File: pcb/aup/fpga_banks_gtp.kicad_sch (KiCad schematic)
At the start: 1 part, among them U1 XC7A50T-2FGG484C

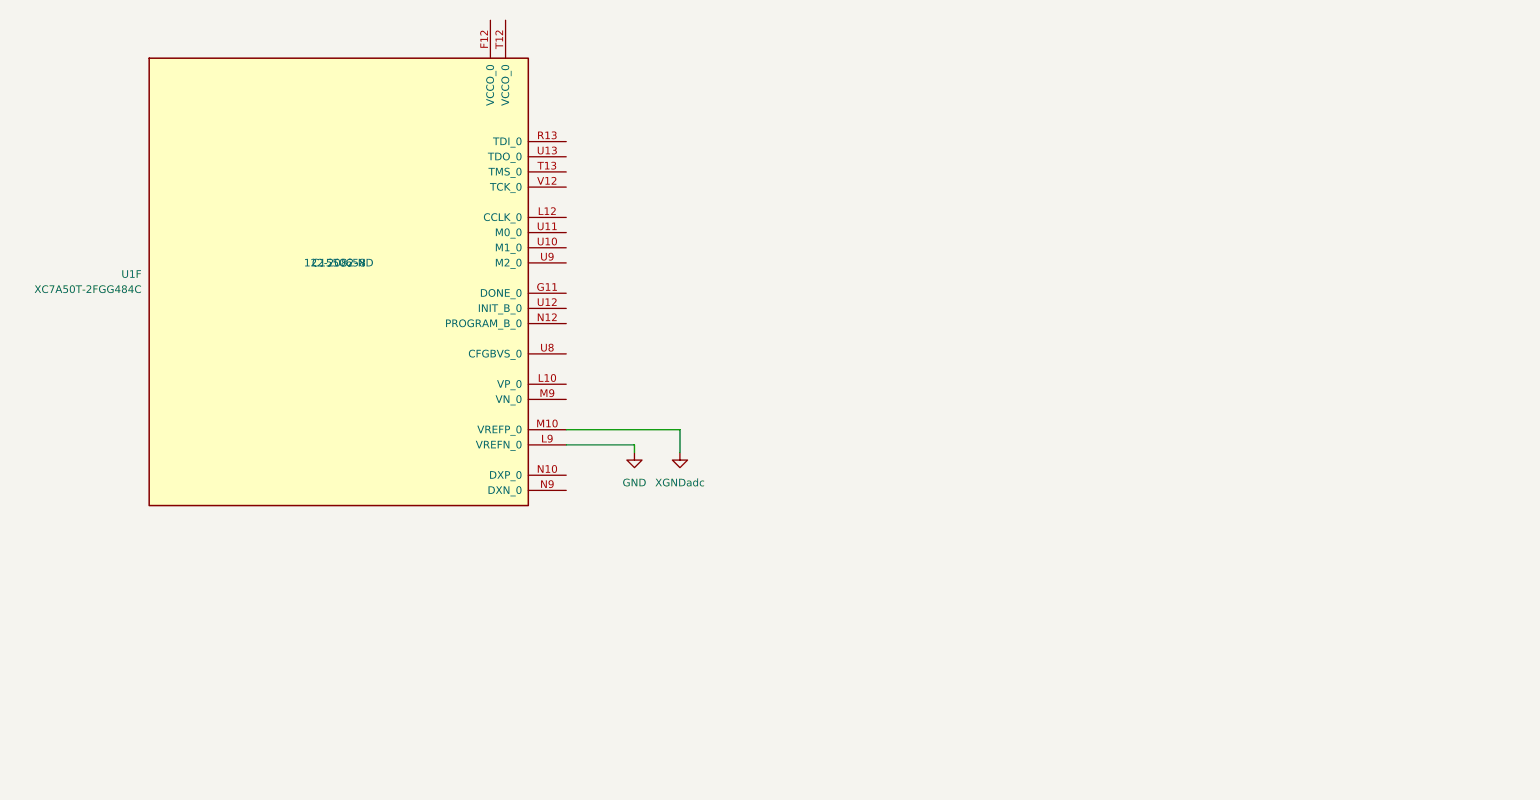
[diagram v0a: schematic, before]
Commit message: Add hierarchical sheets for banks and add caps.
There are some stale sheets in this commit, but I don't want to delete
an active one accidentally. Save them all for now, and then go back and
clean them up.
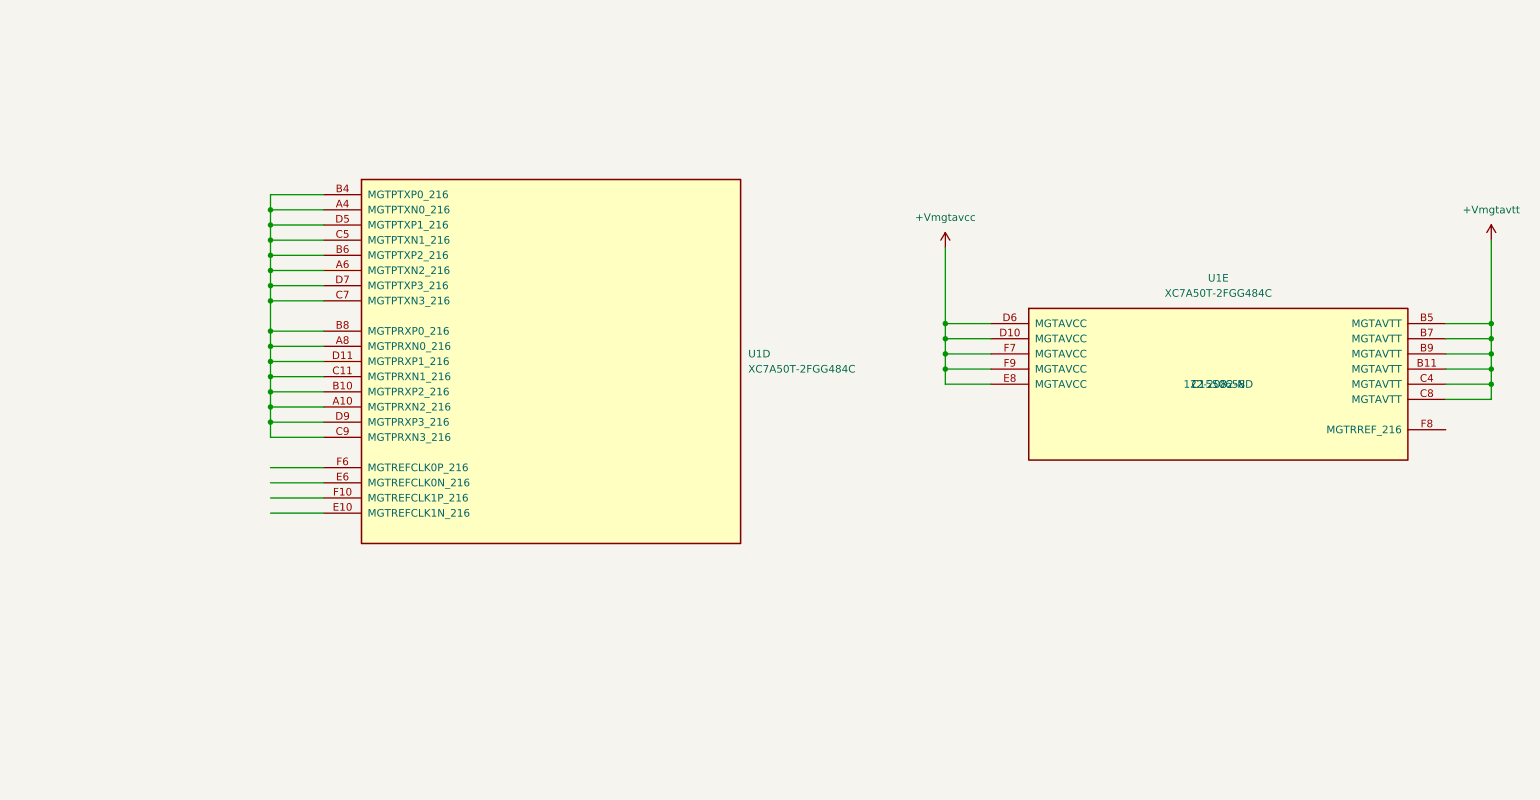
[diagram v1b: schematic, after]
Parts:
- removed U1: XC7A50T-2FGG484C, !Xilinx:Xilinx_FGG484, symbol !Xilinx:XC7A50T-FGG484
- added U1: XC7A50T-2FGG484C, !Xilinx:Xilinx_FGG484, symbol !Xilinx:XC7A50T-FGG484
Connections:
- new net: U1.A10 (MGTPRXN2_216), U1.A4 (MGTPTXN0_216), U1.A6 (MGTPTXN2_216), U1.A8 (MGTPRXN0_216), U1.B10 (MGTPRXP2_216), U1.B4 (MGTPTXP0_216), U1.B6 (MGTPTXP2_216), U1.B8 (MGTPRXP0_216), U1.C11 (MGTPRXN1_216), U1.C5 (MGTPTXN1_216), U1.C7 (MGTPTXN3_216), U1.C9 (MGTPRXN3_216), U1.D11 (MGTPRXP1_216), U1.D5 (MGTPTXP1_216), U1.D7 (MGTPTXP3_216), U1.D9 (MGTPRXP3_216)
- new net +Vmgtavcc: U1.D10 (MGTAVCC), U1.D6 (MGTAVCC), U1.E8 (MGTAVCC), U1.F7 (MGTAVCC), U1.F9 (MGTAVCC)
- new net +Vmgtavtt: U1.B11 (MGTAVTT), U1.B5 (MGTAVTT), U1.B7 (MGTAVTT), U1.B9 (MGTAVTT), U1.C4 (MGTAVTT), U1.C8 (MGTAVTT)

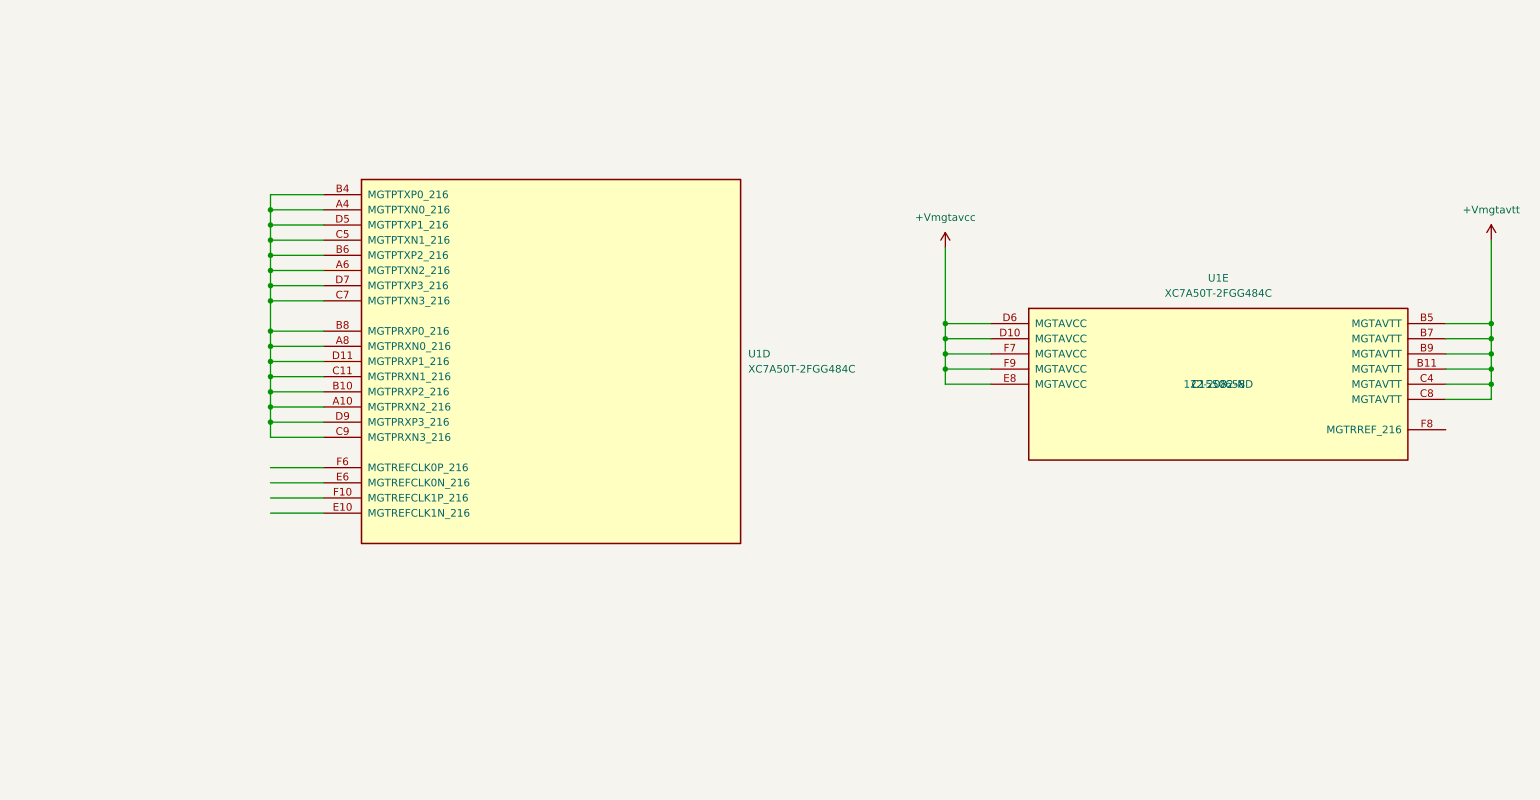
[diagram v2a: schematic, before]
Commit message: Add GTP passives
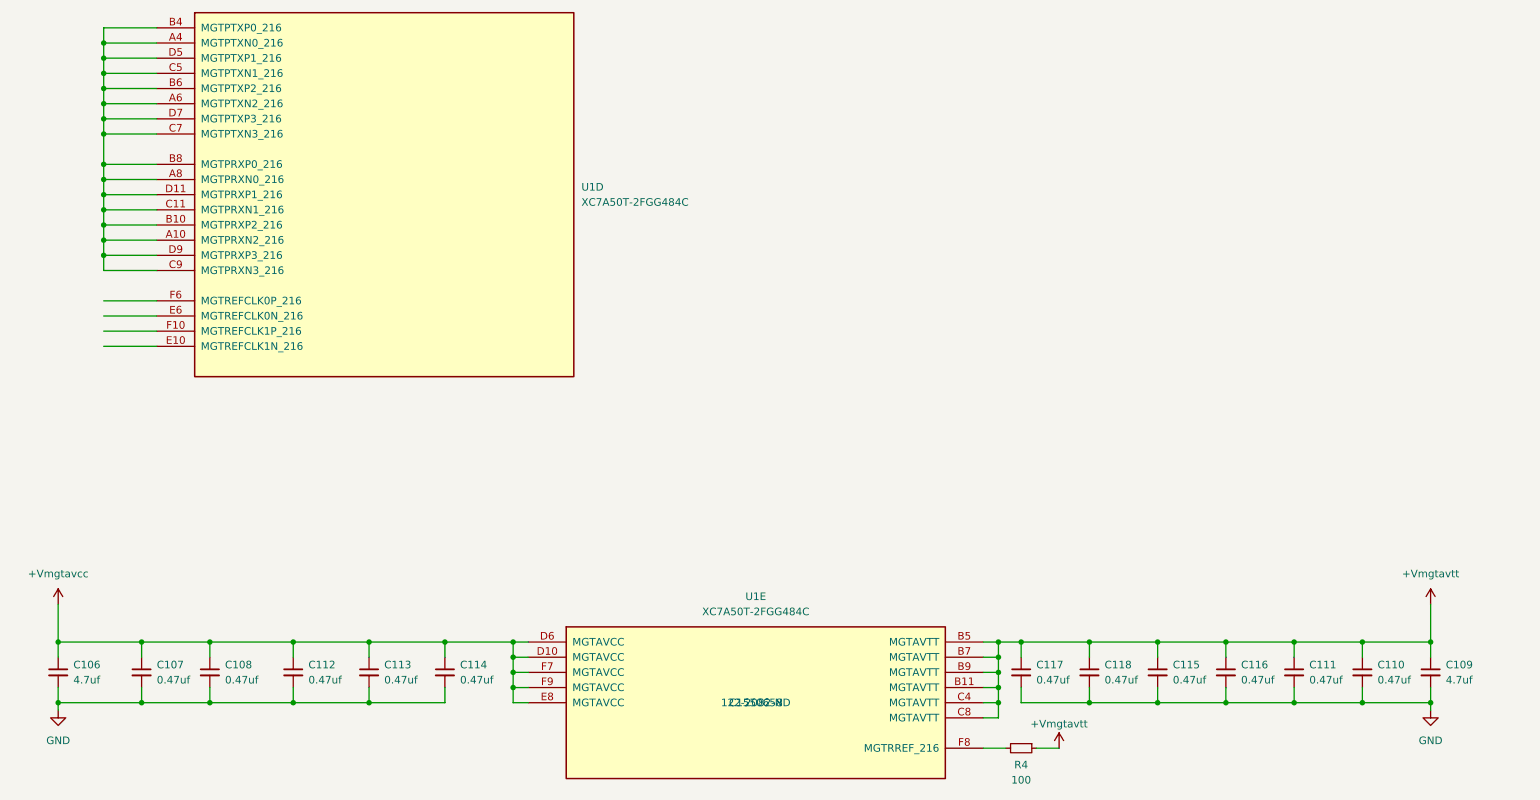
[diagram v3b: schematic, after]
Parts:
- added C106, C109: 4.7uf, Capacitor_SMD:C_0805_2012Metric, symbol !Misc:C_4.7uf_0805
- added C107, C108, C110, C111, C112, C113, C114, C115, C116, C117, C118: 0.47uf, Capacitor_SMD:C_0201_0603Metric, symbol !Misc:C_0.47uf_0201
- added R4: 100, Resistor_SMD:R_0201_0603Metric, symbol !Misc:R_100_0201
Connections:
- net +Vmgtavcc: now also C106.1, C107.1, C108.1, C112.1, C113.1, C114.1
- net +Vmgtavtt: now also C109.1, C110.1, C111.1, C115.1, C116.1, C117.1, C118.1, R4.1
- net at U1.F8 (MGTRREF_216): now also R4.2
- new net GND: C106.2, C107.2, C108.2, C109.2, C110.2, C111.2, C112.2, C113.2, C114.2, C115.2, C116.2, C117.2, C118.2
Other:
- moved on the sheet: U1D, U1E

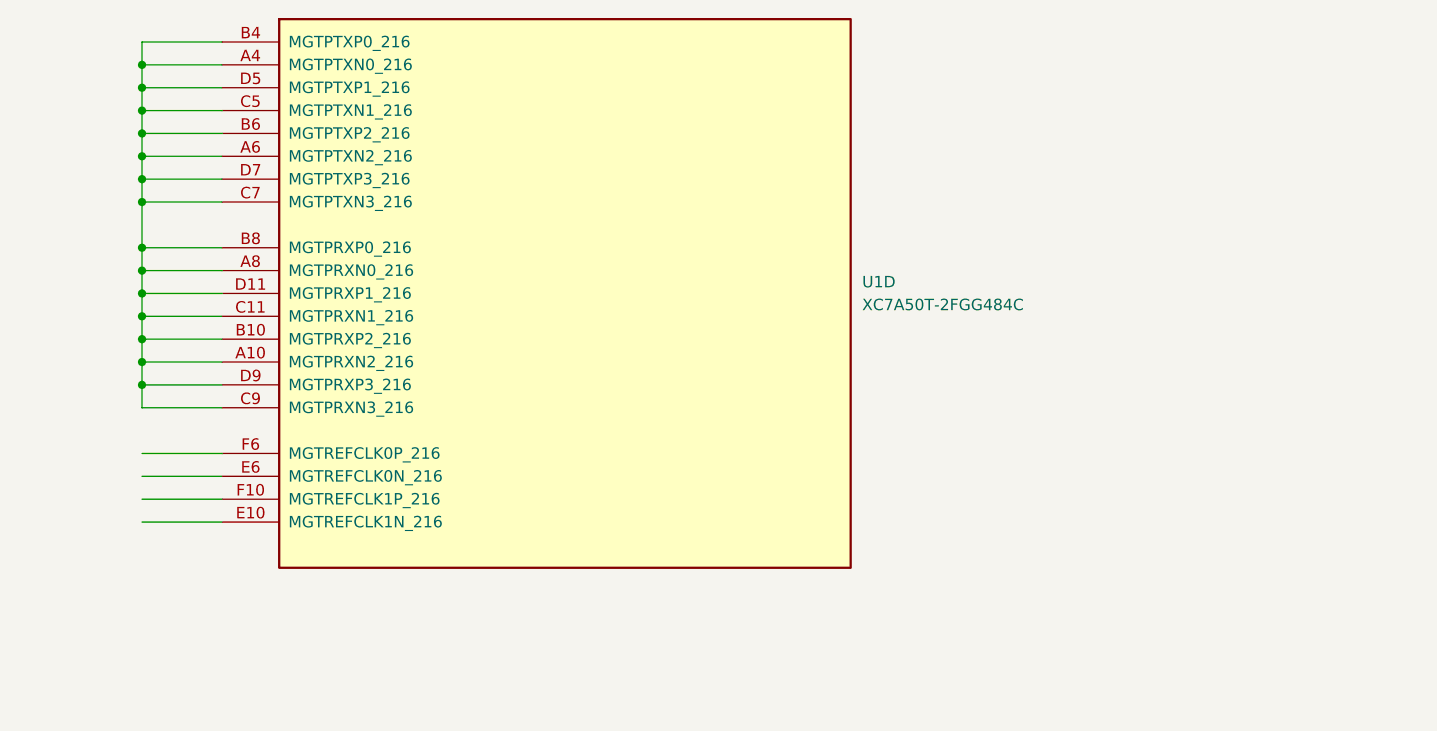
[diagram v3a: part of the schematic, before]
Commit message: Start working out GTP diff pair routing
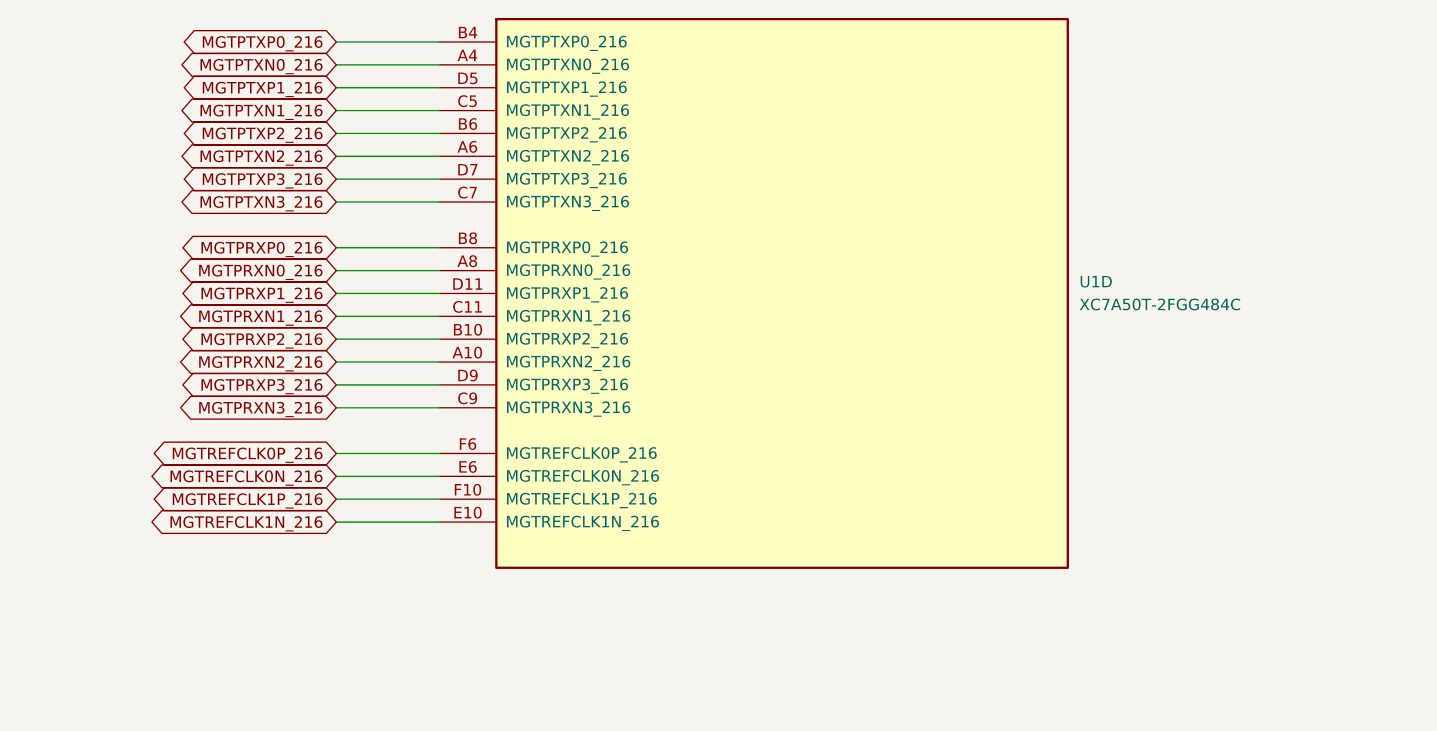
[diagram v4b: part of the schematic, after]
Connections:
- net MGTREFCLK1N_216: now reaches U1.E10 (MGTREFCLK1N_216)
- net MGTREFCLK0N_216: now reaches U1.E6 (MGTREFCLK0N_216)
- net MGTREFCLK1P_216: now reaches U1.F10 (MGTREFCLK1P_216)
- net MGTREFCLK0P_216: now reaches U1.F6 (MGTREFCLK0P_216)
- new net MGTPRXN0_216: U1.A8 (MGTPRXN0_216)
- new net MGTPRXN1_216: U1.C11 (MGTPRXN1_216)
- new net MGTPRXN2_216: U1.A10 (MGTPRXN2_216)
- new net MGTPRXN3_216: U1.C9 (MGTPRXN3_216)
- new net MGTPRXP0_216: U1.B8 (MGTPRXP0_216)
- new net MGTPRXP1_216: U1.D11 (MGTPRXP1_216)
- new net MGTPRXP2_216: U1.B10 (MGTPRXP2_216)
- new net MGTPRXP3_216: U1.D9 (MGTPRXP3_216)
- new net MGTPTXN0_216: U1.A4 (MGTPTXN0_216)
- new net MGTPTXN1_216: U1.C5 (MGTPTXN1_216)
- new net MGTPTXN2_216: U1.A6 (MGTPTXN2_216)
- new net MGTPTXN3_216: U1.C7 (MGTPTXN3_216)
- new net MGTPTXP0_216: U1.B4 (MGTPTXP0_216)
- new net MGTPTXP1_216: U1.D5 (MGTPTXP1_216)
- new net MGTPTXP2_216: U1.B6 (MGTPTXP2_216)
- new net MGTPTXP3_216: U1.D7 (MGTPTXP3_216)
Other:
- moved on the sheet: U1D

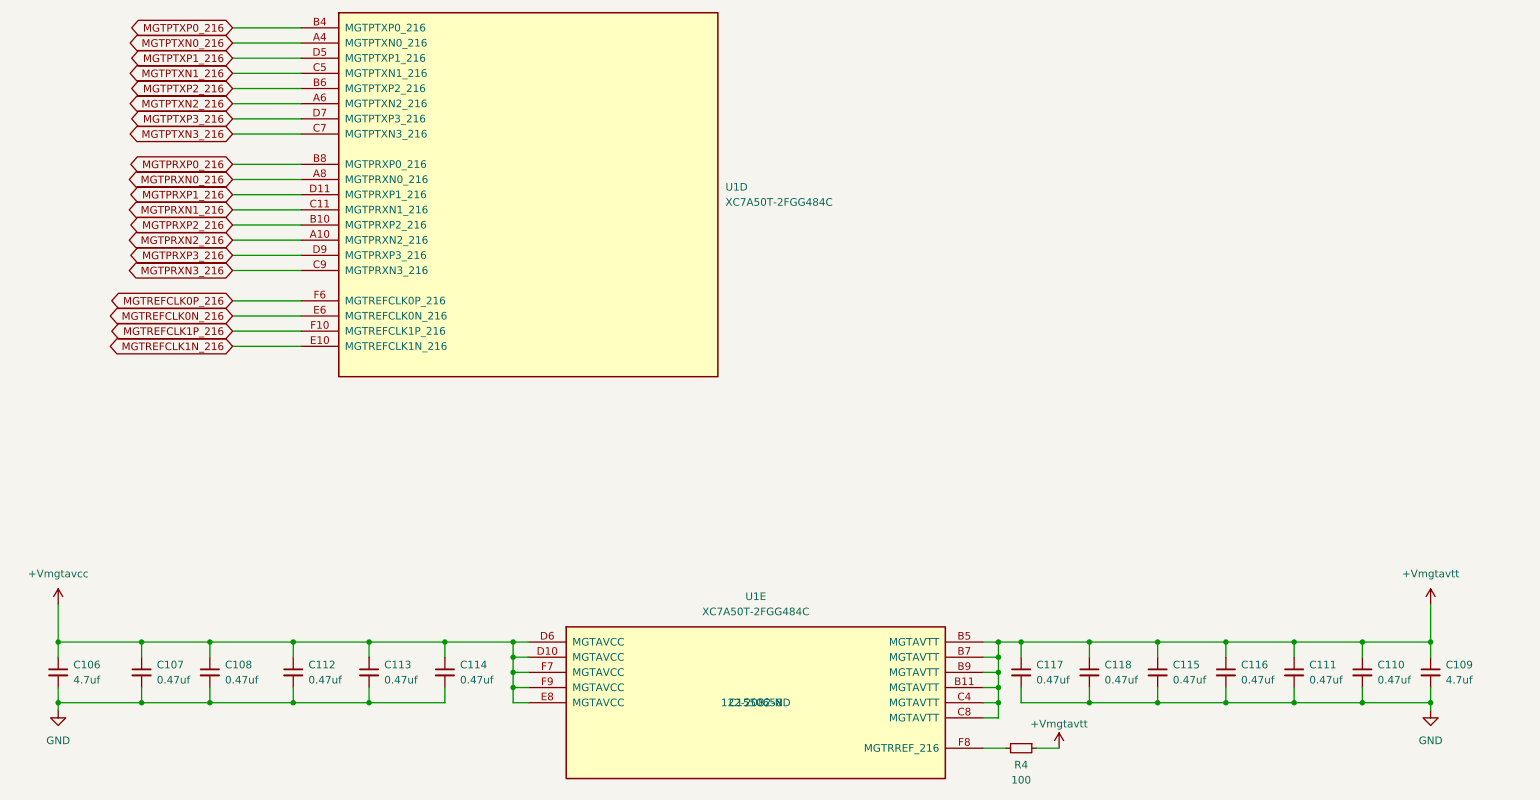
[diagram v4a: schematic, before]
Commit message: GTP diff pairs routed, but not tuned
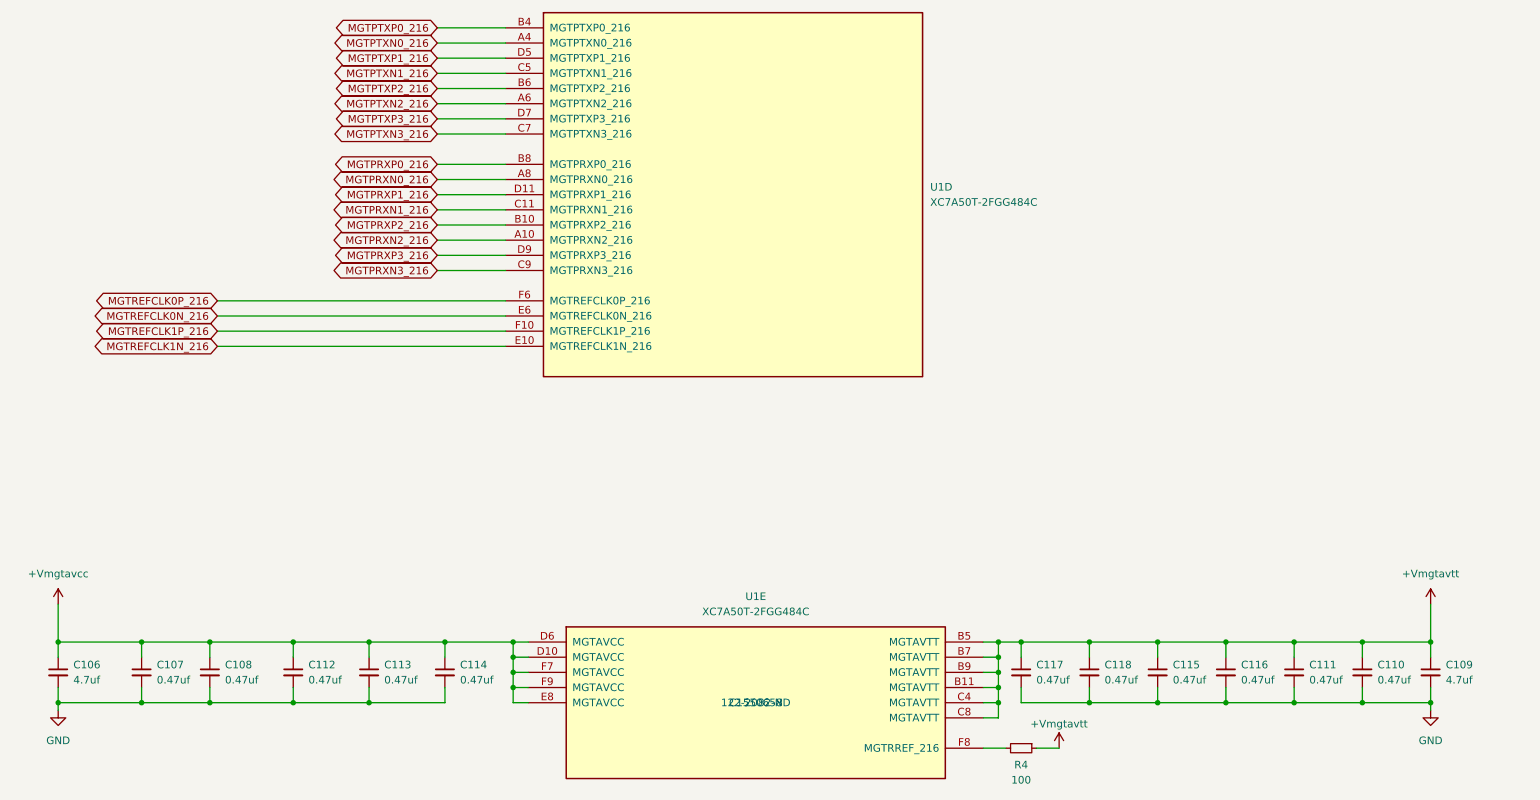
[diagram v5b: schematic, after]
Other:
- moved on the sheet: U1D
